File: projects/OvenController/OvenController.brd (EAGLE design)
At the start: 160 x 100 mm, 47 parts, among them IC1 ESP32-WROOM-32U, K1 EB2-5NU, K2 EB2-5NU, K3 EB2-5NU, K4 EB2-5NU, K5 EB2-5NU, Q2 MBT3904DW1T1, U1 LTV-816_OPTO_ISOLATOR", U3 AP2112K-3.3V, U4 CP2102N

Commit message: Updated schematic and semi-final layout.
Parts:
- removed D1, D4, D5, D6, D7: 3A/40V/500mV, SparkFun-DiscreteSemi:SMA-DIODE
- removed FD1, FD2, FD3, FD4: FIDUCIALUFIDUCIAL, SparkFun-Aesthetics:FIDUCIAL-MICRO
- removed FRAME1: FRAME-LEDGER, SparkFun-Aesthetics:CREATIVE_COMMONS
- removed H1, H2: STAND-OFFTIGHT, SparkFun-Hardware:STAND-OFF-TIGHT
- removed K4, K5: EB2-5NU, SamacSysImported:EB2-5NU
- removed LOGO1: SFE_LOGO_FLAME.1_INCH, SparkFun-Aesthetics:SFE_LOGO_FLAME_.1
- removed LOGO2: OSHW-LOGOMINI, SparkFun-Aesthetics:OSHW-LOGO-MINI
- removed LOGO3: SFE_LOGO_NAME_FLAME.1_INCH, SparkFun-Aesthetics:SFE_LOGO_NAME_FLAME_.1
- removed U$21, U$22, U$24: SSM6N7002KFU, tew-transistors:SOT363_INFINEON
- added R10, R11, R12, R6, R9: 301, SparkFun-Resistors:0603
- added R13: 300, rcl:R1210W
- K1, K2, K3: value EB2-5NU -> CPC2030N; device SamacSysImported:EB2-5NU -> SamacSysImported:SOP254P610X218-8N
- R5: value 604 -> 300; device SparkFun-Resistors:0603 -> rcl:R1210W
- moved C7 56.5 mm to (46.7, 4.76), turned to 270 degrees
- moved D2 49.3 mm to (43.2, 4.45), turned to 270 degrees
- moved C1 49.2 mm to (37.5, 4.45), turned to 180 degrees
- moved C10 43.2 mm to (37.5, 7.30), turned to 180 degrees
- moved R1 41.9 mm to (2.22, 15.2), turned to 90 degrees
- moved R5 40.2 mm to (54.3, 14.6), turned to 0 degrees
- moved R2 38.6 mm to (2.22, 11.1), turned to 90 degrees
- moved S1 37.9 mm to (4.13, 7.30)
- moved U1 27.9 mm to (45.7, 15.9), turned to 180 degrees
- moved BAKE 26.5 mm to (42.5, 28.3)
- moved R18 25.6 mm to (8.89, 6.03), turned to 0 degrees
- moved R17 24.3 mm to (11.7, 9.21)
- moved Q2 23.7 mm to (8.26, 9.53), turned to 180 degrees
- moved BTN_CONN 22.4 mm to (73.7, 18.4)
- moved R3 21.7 mm to (37.5, 11.4)
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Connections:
- removed net K1_COIL-: D1.A, K1.10, U$21.6
- removed net K2_COIL-: D4.A, K2.10, U$22.6
- removed net K3_COIL-: D6.A, K3.10, U$22.3
- removed net K4_COIL-: D7.A, K4.10, U$21.3
- removed net K5_COIL-: D5.A, K5.10, U$24.6
- removed net N$7 (its old number): BAKE.2, R5.2
- new net !BAKE_ON: IC1.29, R3.1, U1.4
- new net CONTROL_+_2: K3.3
- new net CONTROL_-_2: K3.4
- new net N$11: K2.2, R10.2
- new net N$13: K2.4, R11.2
- new net N$14: K3.2, R12.2
- new net N$5: R13.1, R5.2
- new net N$8: K1.2, R6.2
- new net N$9: K1.4, R9.2
- net BTN1_1: now also K1.5; no longer K1.3
- net BTN1_2: now also K1.6; no longer K1.4
- net BTN2_1: now also K1.7; no longer K2.3
- net BTN2_2: now also K1.8; no longer K2.4
- net BTN3_1: now also K2.5; no longer K3.3
- net BTN3_2: now also K2.6; no longer K3.4
- net BTN4_1: now also K2.7; no longer K4.3
- net BTN4_2: now also K2.8; no longer K4.4
- net BTN5_1: now also K3.5; no longer K5.3
- net BTN5_2: now also K3.6; no longer K5.4
- net GND: now also R10.1, R11.1, R12.1, R6.1, R9.1; no longer U$21.1, U$21.4, U$22.1, U$22.4, U$24.1, U$24.4, U$24.5
- net K1_CTRL: now also K1.1; no longer U$21.2
- net K2_CTRL: now also K1.3; no longer U$22.2
- net K3_CTRL: now also K2.1; no longer U$22.5
- net K4_CTRL: now also K2.3; no longer U$21.5
- net K5_CTRL: now also K3.1; no longer U$24.2
- net N$4: now also BAKE.2, R13.2; no longer R3.1, U1.4
- net V_USB: no longer D1.C, D4.C, D5.C, D6.C, D7.C, K1.1, K2.1, K3.1, K4.1, K5.1
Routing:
- net 3.3V: track 6.01 -> 72.4 mm, vias 0 -> 3
- net V_USB: track 8.61 -> 60.8 mm, vias 2 -> 3
- net RTS: track 59.3 -> 15.1 mm, vias 0 -> 2
- net !BAKE_ON: track 0.00 -> 32.5 mm, vias 0 -> 2
- net K4_CTRL: track 12.8 -> 42.1 mm, vias 0 -> 2
- net N$5: track 0.00 -> 28.4 mm, vias 0 -> 2
- net 0: track 0.00 -> 28.0 mm, vias 0 -> 2
- net BTN3_1: track 0.00 -> 26.4 mm, vias 0 -> 1
- net CHIP_PU: track 24.6 -> 42.8 mm, vias 2 -> 0
- net K1_CTRL: track 13.7 -> 31.5 mm, vias 2 -> 0
- net BTN5_2: track 0.00 -> 17.8 mm, vias 0 -> 1
- net BTN5_1: track 0.00 -> 17.8 mm
- net BTN4_2: track 0.00 -> 17.1 mm, vias 0 -> 1
- net K3_CTRL: track 19.3 -> 34.6 mm, vias 0 -> 2
- net BTN4_1: track 0.00 -> 15.0 mm, vias 0 -> 1
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- added copper zone on layer 16, net GND
- removed copper zone on layer 16, net V_USB
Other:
- board size 160 x 100 mm -> 81.9 x 35.6 mm

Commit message: OvenController v1.0 as ordered.
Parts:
- C10: device SparkFun-Capacitors:0402 -> SparkFun-Capacitors:0603
- J5: value (none) -> UJ2-MIBH2-4-SMT-TR; device SparkFun-Connectors:USB-MICROB-PTH-MILL -> tew-connectors:UJ2-MIBH2-4-SMT-TR
- R8: value 100K -> 100k; device SparkFun-Resistors:0402 -> SparkFun-Resistors:0603
- moved S2 2.31 mm to (22.5, 30.2)
- moved J5 0.64 mm to (5.08, 23.5), turned to 0 degrees
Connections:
- net D+: now also J5.P3; no longer J5.D+
- net D-: now also J5.P2; no longer J5.D-
- net GND: now also J5.B1, J5.B2, J5.B3, J5.B4, J5.B5, J5.P5; no longer J5.GND
- net V_USB: now also J5.P1; no longer J5.VBUS
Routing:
- net 0: track 28.0 -> 29.3 mm
- net GND: track 2.36 -> 3.52 mm, vias 24 -> 34
- net D-: track 16.5 -> 17.3 mm
- net D+: track 17.2 -> 18.0 mm
- net K2_CTRL: track 31.2 -> 30.7 mm
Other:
- board text added: "Oven Controller v1.0 Thomas Willson"

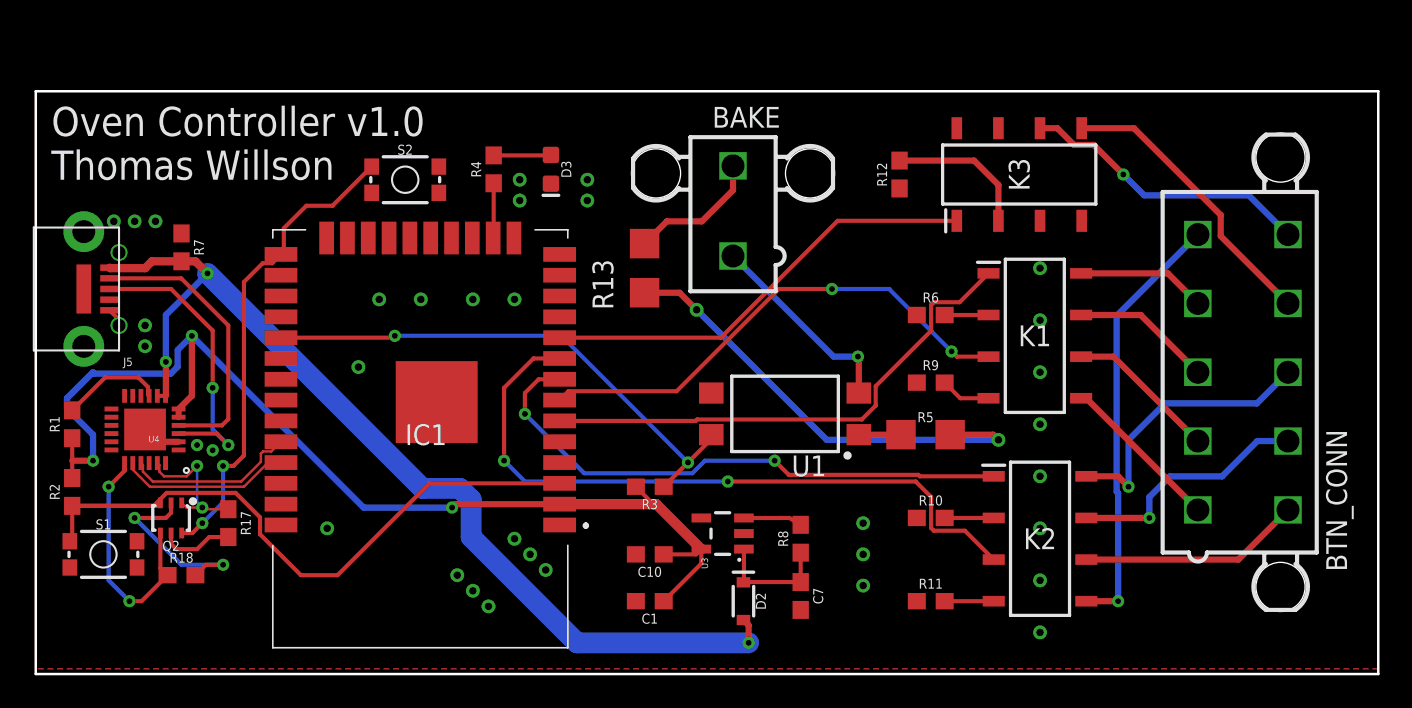
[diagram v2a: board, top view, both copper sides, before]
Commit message: Oven Controller v1.1
Added JTAG header.
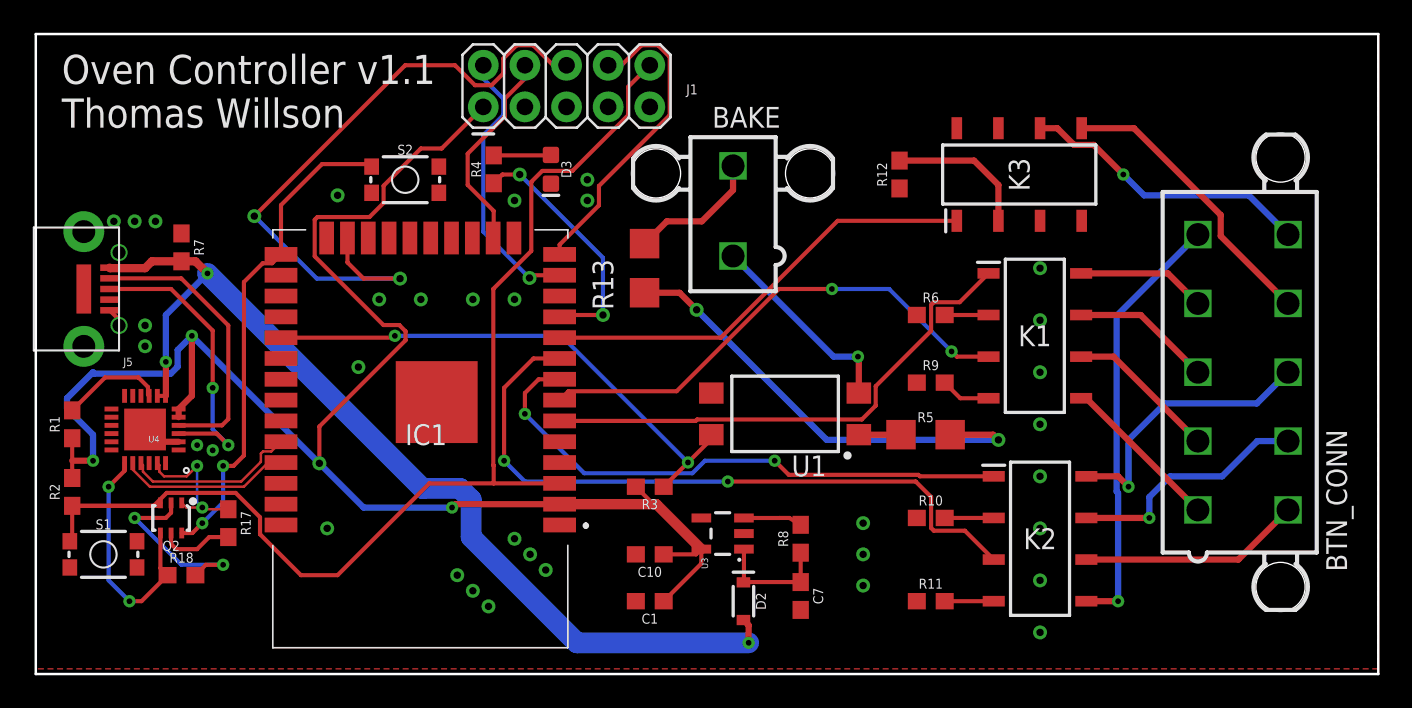
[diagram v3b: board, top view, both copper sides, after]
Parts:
- added J1: (no value), SparkFun-Connectors:2X5
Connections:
- removed net 13: IC1.16, R4.1
- new net LED: IC1.11, R4.1
- new net TCK: IC1.16, J1.4
- new net TDI: IC1.14, J1.8
- new net TDO: IC1.23, J1.6
- new net TMS: IC1.13, J1.2
- net 3.3V: now also J1.1
- net CHIP_PU: now also J1.10
- net GND: now also J1.3, J1.9
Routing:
- net TDO: track 0.00 -> 41.0 mm, vias 0 -> 2
- net 3.3V: track 72.1 -> 105.8 mm, vias 3 -> 4
- net CHIP_PU: track 42.8 -> 73.3 mm
- net TDI: track 0.00 -> 19.4 mm
- net TMS: track 0.00 -> 17.1 mm, vias 0 -> 1
- net LED: track 0.00 -> 15.2 mm, vias 0 -> 2
- net TCK: track 0.00 -> 12.7 mm
- net 13: track 3.36 -> 0.00 mm
- net 0: track 29.3 -> 30.2 mm
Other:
- board size 81.9 x 35.6 mm -> 81.9 x 39.1 mm
- board text added: "Oven Controller v1.1 Thomas Willson"
- board text removed: "Oven Controller v1.0 Thomas Willson"

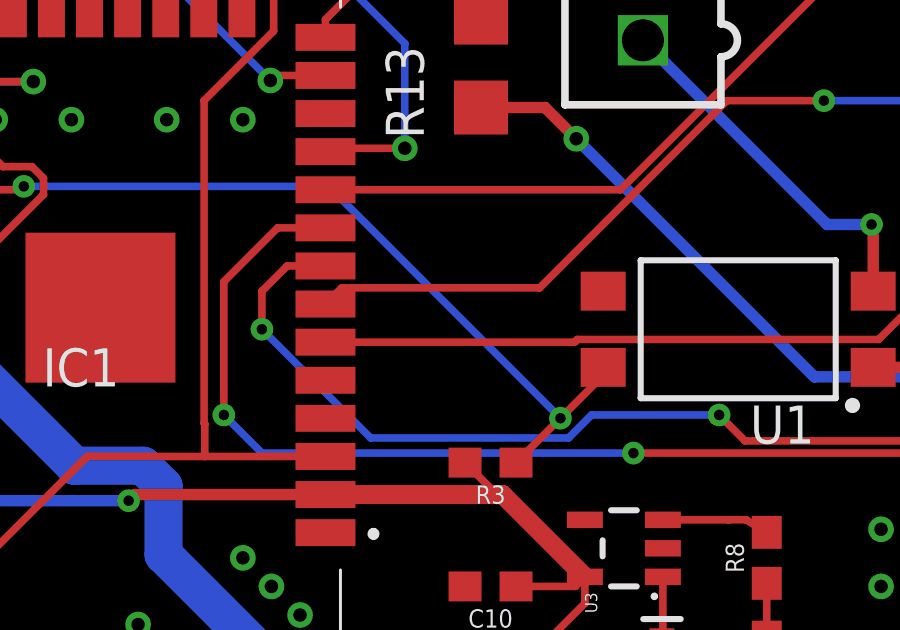
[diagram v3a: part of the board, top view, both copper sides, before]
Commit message: Schematic revisions based on build. Layout needs update.
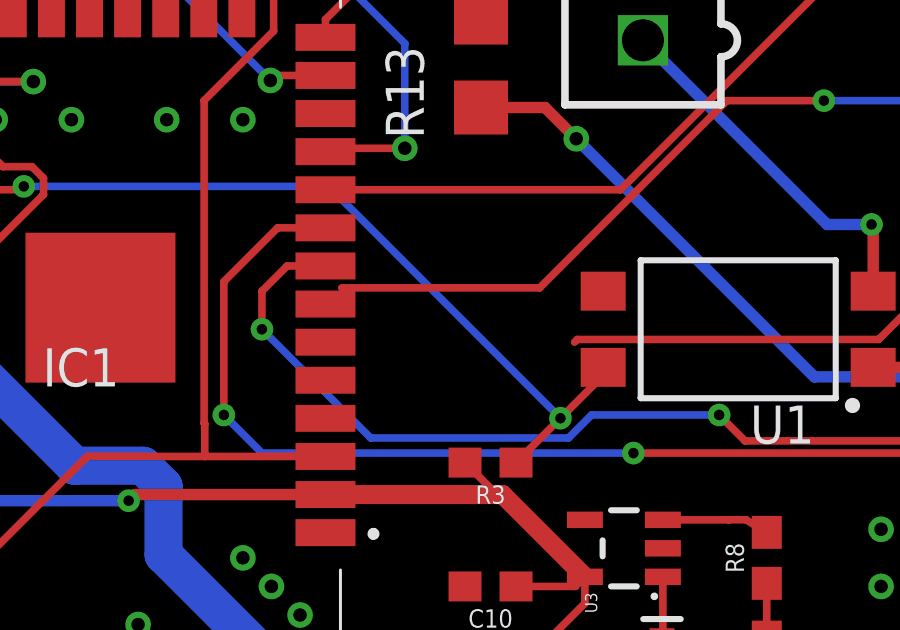
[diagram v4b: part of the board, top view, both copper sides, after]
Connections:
- net K1_CTRL: now also IC1.27; no longer IC1.6
- net K2_CTRL: now also IC1.31; no longer IC1.7
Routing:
- net K1_CTRL: track 31.5 -> 23.2 mm
- net K2_CTRL: track 30.7 -> 29.9 mm
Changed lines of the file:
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@@
 </signal>
 <signal name="K1_CTRL">
-<contactref element="IC1" pad="6"/>
 <contactref element="K1" pad="1"/>
 <wire x1="54.79426875" y1="22.6869" x2="54.6306" y2="22.52323125" width="0.254" layer="1"/>
 <wire x1="51.2494" y1="17.5619" x2="51.2494" y2="16.37926875" width="0.254" layer="1"/>
 <wire x1="40.35426875" y1="15.5344" x2="40.26486875" y2="15.445" width="0.254" layer="1"/>
-<wire x1="40.26486875" y1="15.445" x2="31.9625" y2="15.445" width="0.254" layer="1"/>
 <wire x1="58.135" y1="24.4475" x2="56.3744" y2="22.6869" width="0.254" layer="1"/>
 <wire x1="54.6306" y1="20.9431" x2="51.2494" y2="17.5619" width="0.254" layer="1"/>
@@
 <wire x1="51.2494" y1="16.37926875" x2="50.40453125" y2="15.5344" width="0.254" layer="1"/>
 <wire x1="50.40453125" y1="15.5344" x2="40.35426875" y2="15.5344" width="0.254" layer="1"/>
+<contactref element="IC1" pad="27"/>
+<wire x1="14.9625" y1="23.065" x2="40.26486875" y2="15.445" width="0" layer="19" extent="1-1"/>
 </signal>
 <signal name="K2_CTRL">
-<contactref element="IC1" pad="7"/>
 <contactref element="K1" pad="3"/>
 <via x="48.5775" y="23.495" extent="1-16" drill="0.35"/>
-<wire x1="31.9625" y1="16.715" x2="32.5031" y2="17.2556" width="0.254" layer="1"/>
 <wire x1="45.3422375" y1="23.495" x2="48.5775" y2="23.495" width="0.254" layer="1"/>
 <wire x1="32.5031" y1="17.2556" x2="39.1028375" y2="17.2556" width="0.254" layer="1"/>
@@
 <wire x1="55.88" y1="19.685" x2="56.1975" y2="19.3675" width="0.254" layer="1"/>
 <wire x1="56.1975" y1="19.3675" x2="58.135" y2="19.3675" width="0.254" layer="1"/>
+<contactref element="IC1" pad="31"/>
+<wire x1="14.9625" y1="17.985" x2="32.5031" y2="17.2556" width="0" layer="19" extent="1-1"/>
 </signal>
 <signal name="K3_CTRL">
